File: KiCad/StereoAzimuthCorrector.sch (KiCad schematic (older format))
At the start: 36 parts

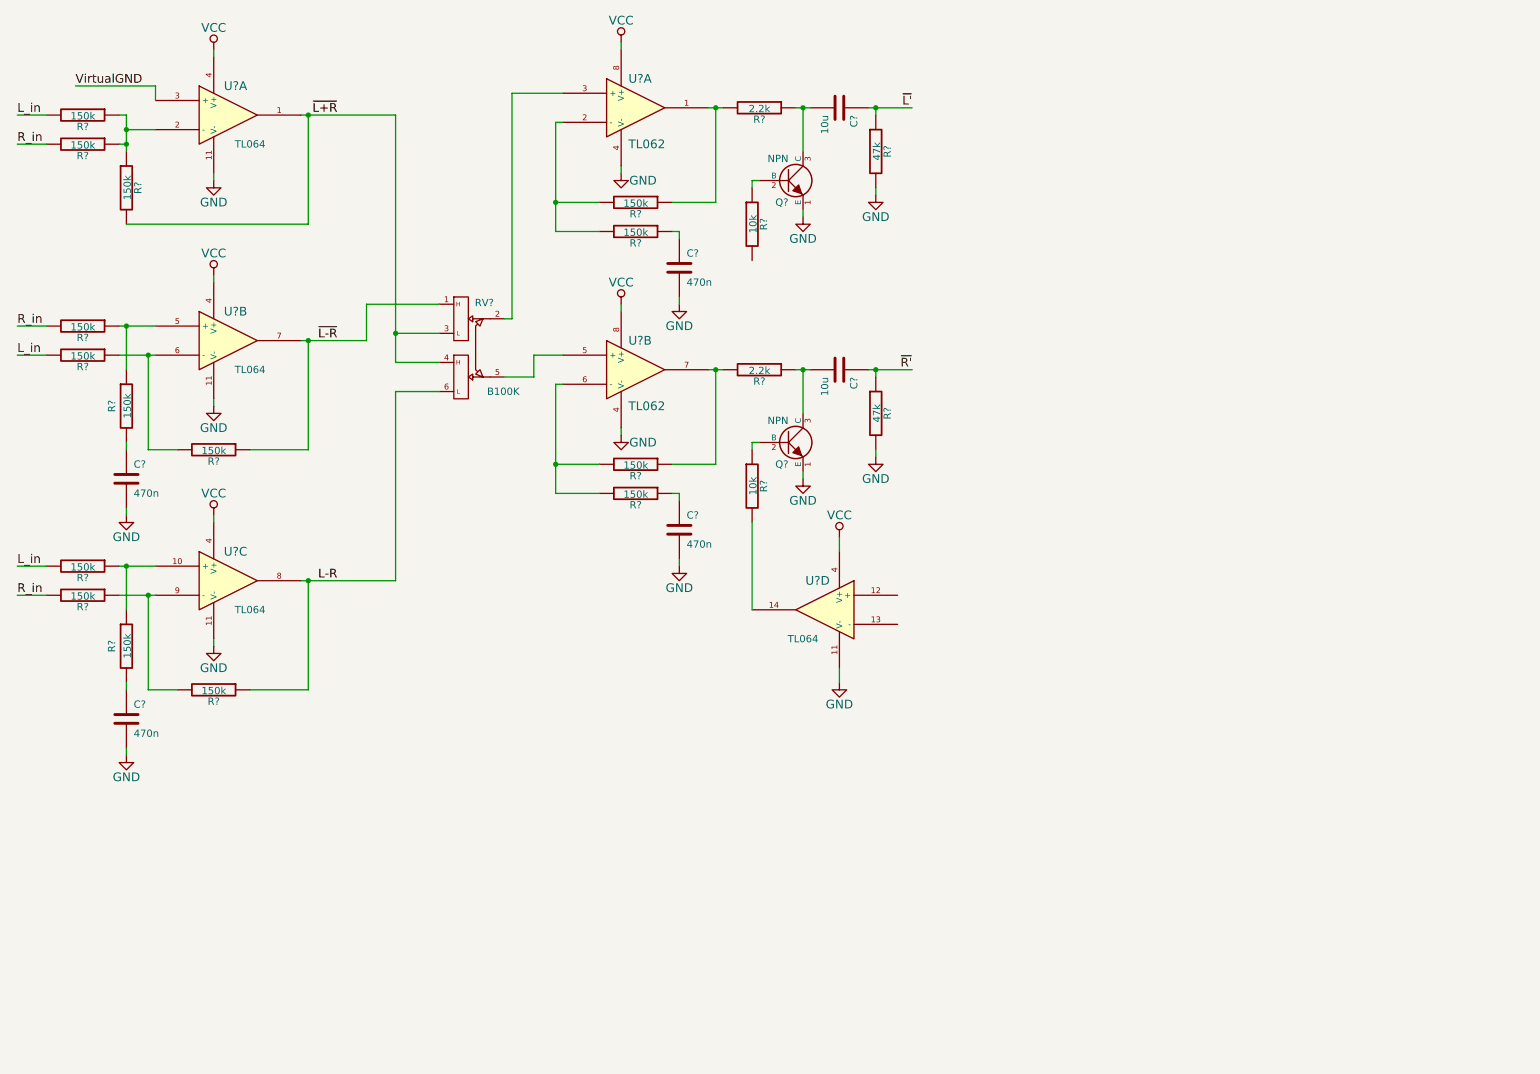
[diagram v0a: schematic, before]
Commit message: Finish main circuitry
Power supply (boost converter) is still TODO
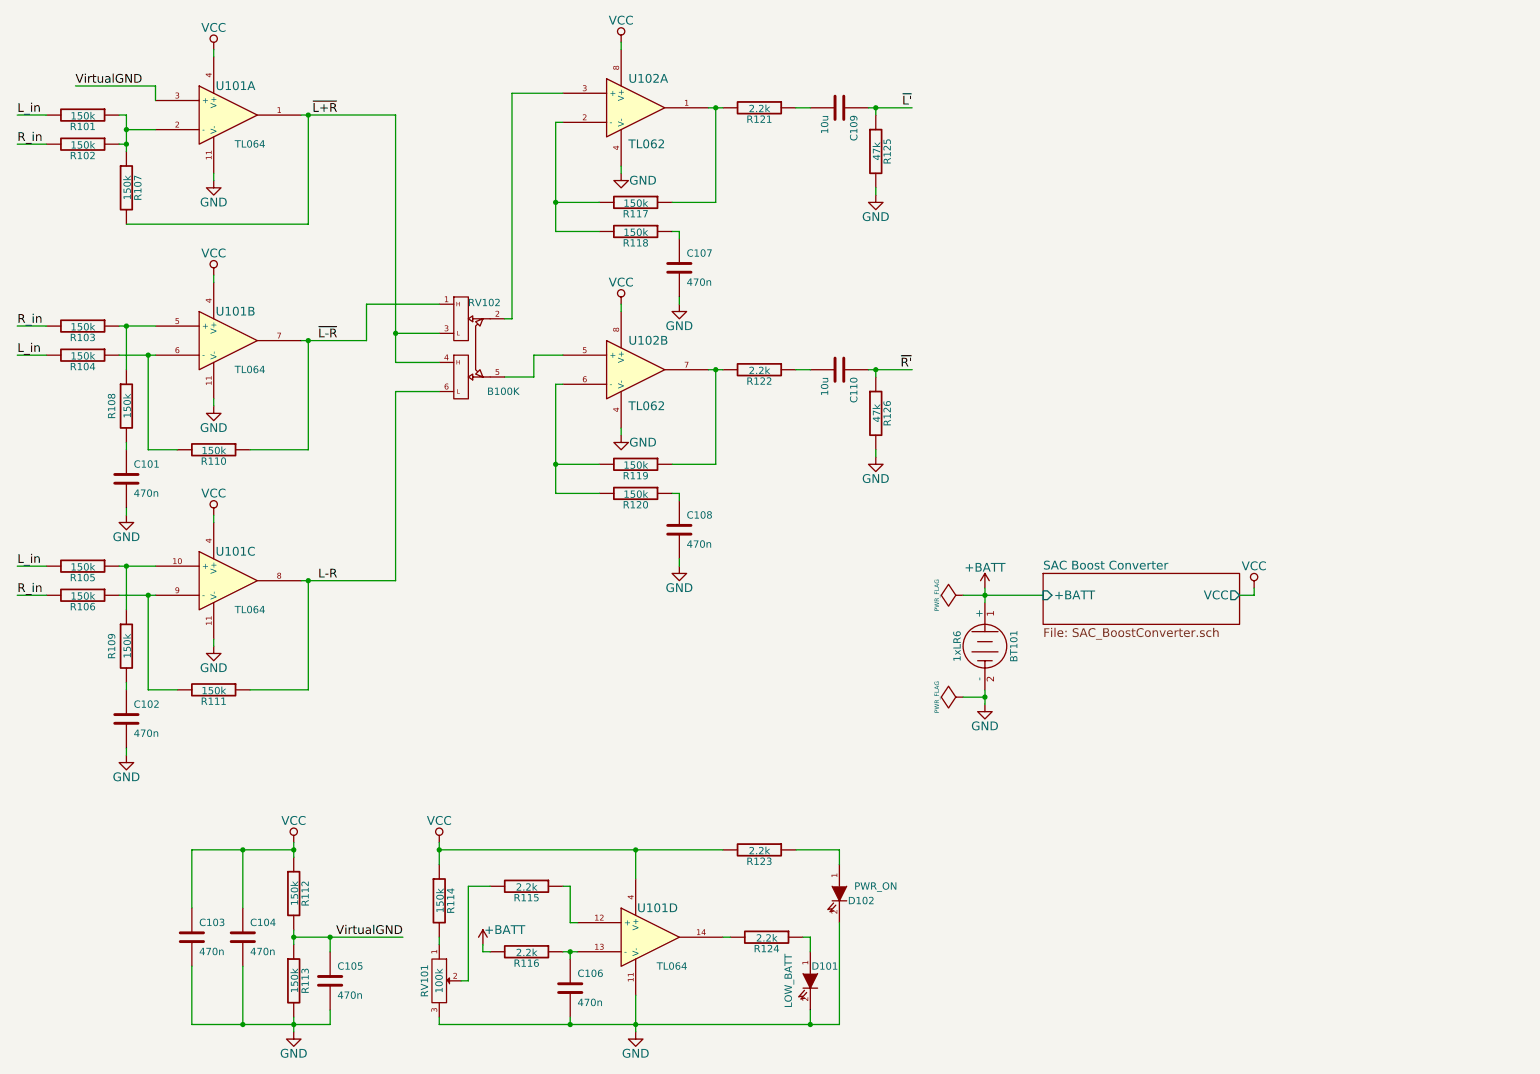
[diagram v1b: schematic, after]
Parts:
- removed Q? (x2): NPN, symbol NPN
- removed R? (x2): 10k, symbol R
- added BT101: 1xLR6, symbol BATTERY
- added C103, C104, C105, C106: 470n, symbol C
- added D101: LOW_BATT, symbol LED
- added D102: PWR_ON, symbol LED
- added R112, R113, R114: 150k, symbol R
- added R115, R116, R123, R124: 2.2k, symbol R
- added RV101: 100k, symbol POT
- gave numbers to parts that had none: 28
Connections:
- net GND: now also BT101.2 (-), C103.2, C104.2, C105.2, C106.2, D101.2 (K), D102.2 (K), R113.2, RV101.3
- net VCC: now also C103.1, C104.1, R112.1, R114.1, R123.2
- net VirtualGND: now also C105.1, R112.2, R113.1
- net at U101.14: now also R124.2
- net at U101.12 (+): now also R115.1
- net at U101.13 (-): now also C106.1, R116.1
- new net: R114.2, RV101.1
- new net: R115.2, RV101.2
- new net: D101.1 (A), R124.1
- new net: D102.1 (A), R123.1
- new net +BATT: BT101.1 (+), R116.2
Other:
- moved on the sheet: U101D

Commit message: Remove unnecessary sheet
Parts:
- removed C106: 470n, symbol C
- removed R116: 2.2k, symbol R
- BT101: value 1xLR6 -> 2xLR6
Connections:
- net +BATT: now also U101.13 (-)
- net at U101.12 (+): now also R115.2; no longer R115.1
- net at RV101.2: now also R115.1; no longer R115.2
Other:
- note added: "Adjust for LOW_BATT\n@ +BATT < 2.0 V"
- note added: "Angle Control"
- moved on the sheet: C103, C104, C105, D101, D102, R112, R113, R114, R115, R123, R124, RV101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

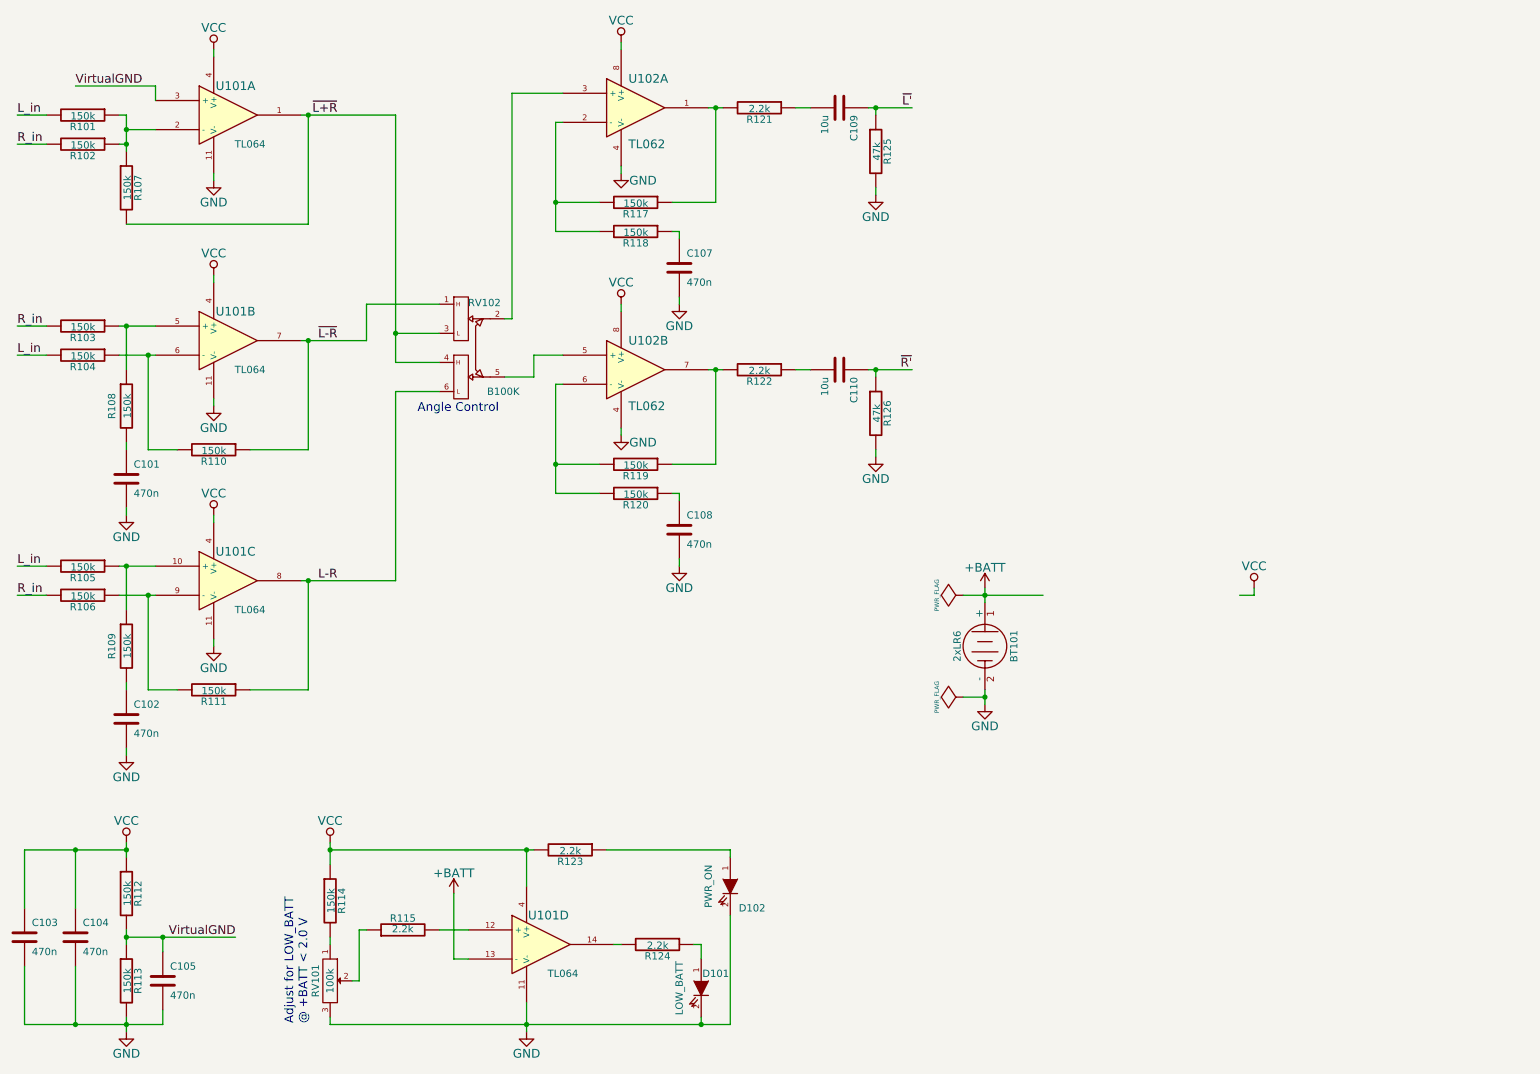
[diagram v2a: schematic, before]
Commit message: Finish power circuitry; begin sourcing parts
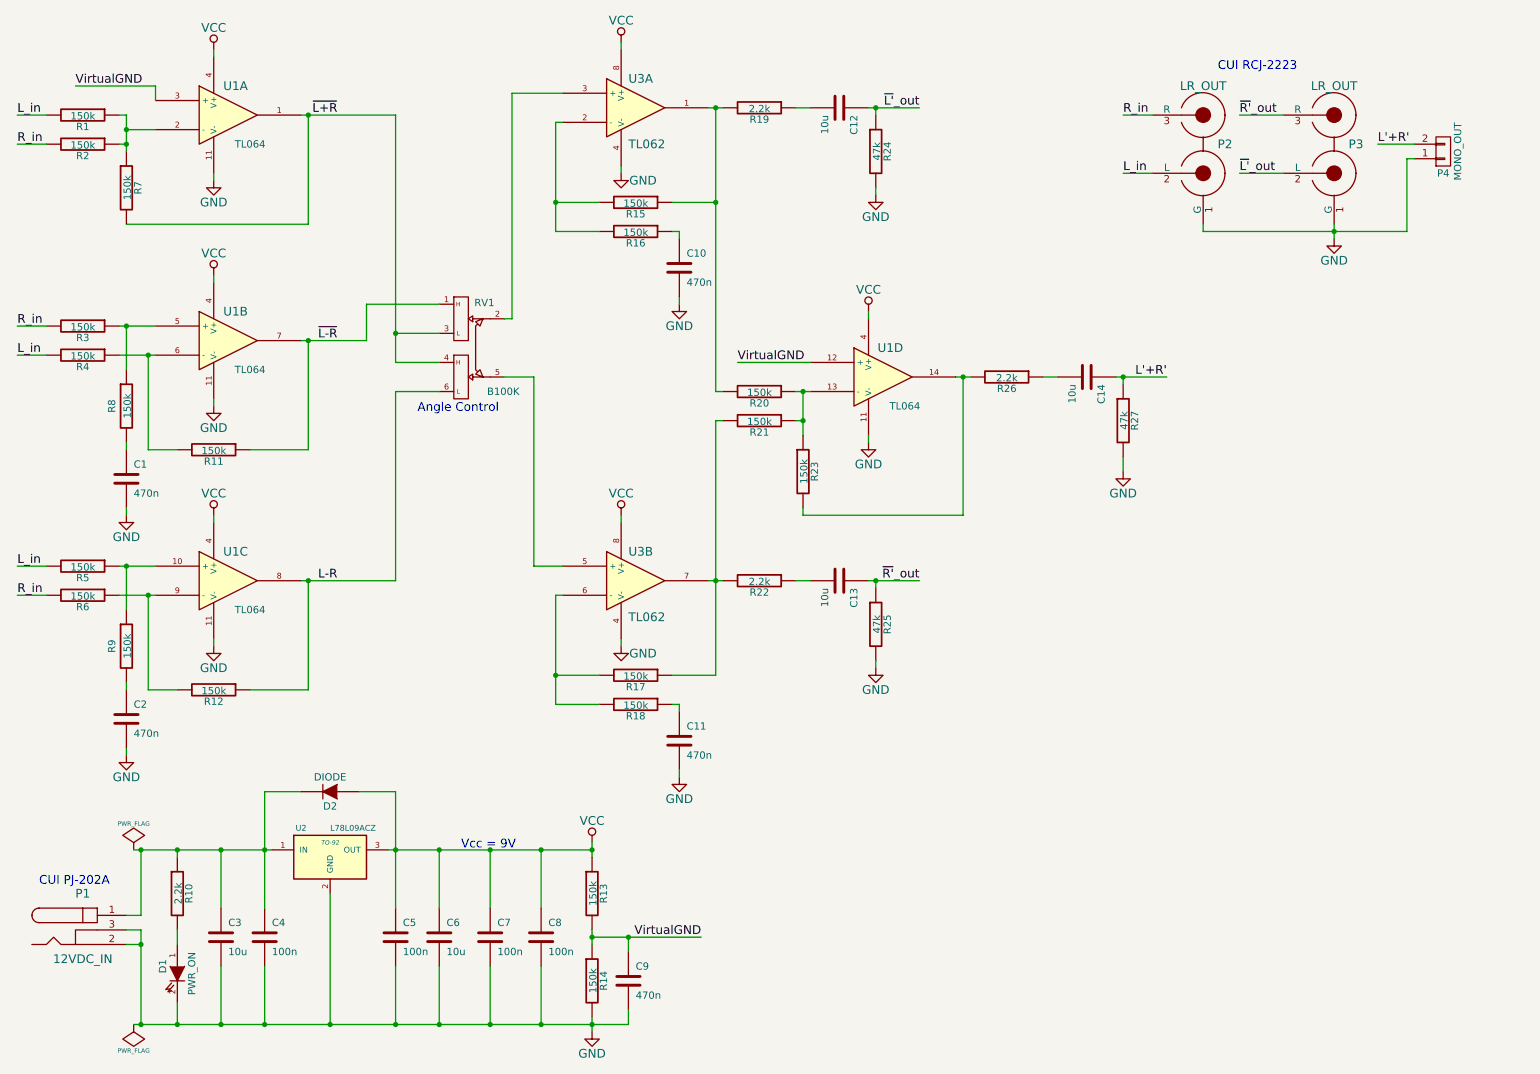
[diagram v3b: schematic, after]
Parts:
- removed BT101: 2xLR6, symbol BATTERY
- removed D101: LOW_BATT, symbol LED
- removed R114: 150k, symbol R
- removed R115, R124: 2.2k, symbol R
- removed RV101: 100k, symbol POT
- added C14, C3, C6: 10u, symbol C
- added C4, C5: 100n, symbol C
- added D2: DIODE, symbol DIODE
- added P1: 12VDC_IN, symbol BARREL_JACK
- added P2, P3: LR_OUT, symbol RCJ-2223
- added P4: MONO_OUT, symbol CONN_01X02
- added R20, R21, R23: 150k, symbol R
- added R26: 2.2k, symbol R
- added R27: 47k, symbol R
- added U2: L78L09ACZ, TO-92, symbol LM7809ACT
- C7: renamed from C103; value 470n -> 100n
- C8: renamed from C104; value 470n -> 100n
- renumbered C101 to C1, C107 to C10, C108 to C11, C109 to C12, C110 to C13, C102 to C2, C105 to C9, D102 to D1, R101 to R1, R123 to R10, R110 to R11, R111 to R12, R112 to R13, R113 to R14, R117 to R15, R118 to R16, R119 to R17, R120 to R18, R121 to R19, R102 to R2, R122 to R22, R125 to R24, R126 to R25, R103 to R3, R104 to R4, R105 to R5, R106 to R6, R107 to R7, R108 to R8, R109 to R9, RV102 to RV1, U101 to U1, U102 to U3
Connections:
- net GND: now also C3.2, C4.2, C5.2, C6.2, P1.2, P1.3, P2.1 (G), P3.1 (G), P4.1 (P1), R27.2, U2.2 (GND)
- net L_in: now also P2.2 (L)
- net R_in: now also P2.3 (R)
- net VCC: now also C5.1, C6.1, D2.1 (A), U2.3 (OUT); no longer R10.2
- net VirtualGND: now also U1.12 (+)
- net at R15.1, R19.2, U3.1: now also R20.2
- net at R17.1, R22.2, U3.7: now also R21.2
- net at U1.14: now also R23.2, R26.2
- net at R10.1: now also C3.1, C4.1, D2.2 (K), P1.1, U2.1 (IN); no longer D1.1 (A)
- net +BATT: no longer names the net of U1.13 (-)
- net +BATT: now also R20.1, R21.1, R23.1
- net ~L' renamed ~L'~_out
- net ~L'~_out: now also P3.2 (L)
- net ~R' renamed ~R'~_out
- net ~R'~_out: now also P3.3 (R)
- new net: C14.2, R26.1
- new net: D1.1 (A), R10.2
- new net L'+R': C14.1, P4.2 (P2), R27.1
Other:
- note added: "CUI PJ-202A"
- note added: "CUI RCJ-2223"
- note added: "Vcc = 9V"
- note removed: "Adjust for LOW_BATT\n@ +BATT < 2.0 V"
- moved on the sheet: C11, C13, C7, C8, C9, D1, R10, R13, R14, R17, R18, R22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
